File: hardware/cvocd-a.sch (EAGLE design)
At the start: 123 parts, among them IC1 LPC812, IC2 AD5696R, IC3 MC14094B, IC4 MC14094B, IC5 LM324D, IC6 REG1117, IC7 6N138, IC8 24LC_64T-I/OT, IC9 MIC5504-2.8YM5-TR

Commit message: rename
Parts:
- removed ACT, PWR, STA: (no value), led:LED3MM
- removed C22: (no value), resistor:CPOL-EUE2.5-5
- removed C23: 100n, rcl:C-EUC0805
- removed C24, C25: (no value), rcl:C-EUC0805
- removed D3, D4, D5: (no value), microbuilder:DIODESOD-123
- removed GT1, GT10, GT11, GT12, GT2, GT3, GT4, GT5, GT6, GT7, GT8, GT9: VERTICAL_3_5MM_SOCKET, jason_eagle6:VERTICAL_3_5MM_SOCKET
- removed IC8: 24LC_64T-I/OT, Microchip-24LCxxx:24LC_64T-I/OT
- removed IC9: MIC5504-2.8YM5-TR, jason_eagle6:MIC5504-2.8YM5-TR
- removed MODE: (no value), switch-omron:10-XX
- removed Q1, Q11, Q13, Q2, Q7, Q9: (no value), microbuilder:MOSFET-P
- removed Q10, Q12, Q14, Q8: (no value), transistor:MMBT3904LT1-NPN-SOT23-BEC
- removed Q3, Q4, Q5, Q6: (no value), jason_eagle6:MOSFET-N_DUAL
- removed R30, R31, R32, R33, R34, R35, R36, R37, R38, R39, R40, R41, R42, R43, R44, R45, R46, R47: (no value), rcl:R-EU_R0805
- added D2: 1N4004, jasons_stuff:1N4004
- added GATE1, GATE10, GATE11, GATE12, GATE2, GATE3, GATE4, GATE5, GATE6, GATE7, GATE8, GATE9: VERTICAL_3_5MM_SOCKET, jason_eagle6:VERTICAL_3_5MM_SOCKET
- added L1, L2, L3: (no value), led:LED3MM
- added S1: (no value), switch-omron:10-XX
- C10, C14, C15: value 100n -> (none)
- C16: device microbuilder:CAP_TANTALUMA/3216_REFLOW -> rcl:C-EUC0805
- C18, C19, C9: value (none) -> 100n
- C20: device rcl:C-EUC0805 -> resistor:CPOL-EUE2.5-5
- IC1: value LPC812 -> PIC16F1825SO14; device jason_eagle6:LPC812 -> jasons_stuff:PIC16F1825SO14
- IC2: value AD5696R -> 74HC595D; device jason_eagle6:AD5696R -> 74xx-eu:74HC595D
- IC3: value MC14094B -> 74HC595D; device jason_eagle6:MC14094B -> 74xx-eu:74HC595D
- IC4: value MC14094B -> MCP4728_QUAD_DAC; device jason_eagle6:MC14094B -> jason_eagle6:MCP4728_QUAD_DAC
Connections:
- removed net 12V: C11.2, C14.1, C22.+, D5.C, IC5P.V+, IC6.VIN, Q1.S, Q2.S, R36.2, R37.2
- removed net 3V3: C15.1, C24.2, IC1.VDD, IC9.VOUT, ICSP.VDD, PWR.A, R4.1
- removed net 5V: C10.1, C16.+, C21.+, C23.1, C25.2, C9.2, D3.A, D4.A, IC2.GAIN, IC2.RESET#, IC2.VDD, IC2.VLOGIC, IC6.VOUT, IC7.VCC, IC8.VCC, IC9.EN, IC9.VIN, R21.1, R22.1, R27.2, R38.2, R39.2
- removed net GT1: C18.1, GT1.4, R40.1, R47.2
- removed net GT1H: IC3.Q4, Q9.G
- removed net GT1L: IC3.Q8, R13.2
- removed net GT1_VSEL: IC1.PIO0_16, Q3G$2.G, R38.1
- removed net GT2: C17.1, GT2.4, R41.1, R44.2
- removed net GT2H: IC3.Q1, Q7.G
- removed net GT2L: IC3.Q5, R14.2
- removed net GT2_VSEL: IC1.PIO0_7, Q3G$1.G, R39.1
- removed net GT3: C20.1, GT3.4, R42.1, R45.2
- removed net GT3H: IC3.Q3, Q13.G
- removed net GT3L: IC3.Q7, R15.2
- removed net GT4: C19.1, GT4.4, R43.1, R46.2
- removed net GT4H: IC3.Q2, Q11.G
- removed net GT4L: IC3.Q6, R16.2
- removed net MODE_SW: IC1.PIO0_17, MODE.S, MODE.S1
- removed net N$10: Q8.B, R14.1
- removed net N$11: Q14.B, R15.1
- removed net N$14: IC3.STROBE, Q6G$2.D, R31.1
- removed net N$17: IC4.Q8, R9.1
- removed net N$18: IC4.Q7, R10.1
- removed net N$19: IC4.Q6, R11.1
- removed net N$38: IC4.Q5, R12.1
- removed net N$44: IC4.Q3, R6.1
- removed net N$45: IC4.Q2, R7.1
- removed net N$54: Q12.C, R46.1
- removed net N$55: Q10.C, R47.1
- removed net N$57: IC1.PIO0_2/TMS, ICSP.ICSP_DAT/PGD
- removed net N$58: IC1.RESET, ICSP.VPP/MCLR, R4.2
- removed net SCL: IC1.PIO0_10, IC2.SCL, IC8.SCL, R22.2
- removed net SDA: IC1.PIO0_11, IC2.SDA, IC8.SDA, R21.2
- removed net VDD_GT1: C13.1, D3.C, IC3.OE, IC3.VDD, Q1.D, Q11.S, Q13.S, Q7.S, Q9.S, R30.2, R31.2, R32.2
- removed net VDD_GT2: C12.1, D4.C, IC4.OE, IC4.VDD, Q2.D, R33.2, R34.2, R35.2
- new net MIDI_OUT: IC1.RC4/TX
- new net N$22: IC1.RC1/SDA/SDI, IC4.SDA, R21.2
- new net N$47: IC2A.QD, R5.1
- new net VDD: C11.2, C12.1, C13.1, C19.2, C20.+, C9.2, IC1.VDD, IC2A.SCL, IC2P.VCC, IC3A.SCL, IC3P.VCC, IC4.VDD, IC6.VOUT, IC7.VCC, ICSP.VDD, L3.A, R21.1, R22.1, R27.2, R4.1
- new net VIN: C10.2, C18.1, C21.+, D2.C, IC5P.V+, IC6.VIN
- net ACT_LED: now also IC1.RA2/INT, L1.A; no longer ACT.A, IC1.PIO0_13
- net GND: now also C10.1, C16.2, C19.1, C20.-, GATE1.2, GATE10.2, GATE11.2, GATE12.2, GATE2.2, GATE3.2, GATE4.2, GATE5.2, GATE6.2, GATE7.2, GATE8.2, GATE9.2, IC2A.G, IC2P.GND, IC3A.G, IC3P.GND, IC4.LDAC#, S1.P, S1.P1; no longer C10.2, C16.-, C19.2, C20.2, C22.-, C23.2, C24.1, C25.1, GT1.2, GT10.2, GT11.2, GT12.2, GT2.2, GT3.2, GT4.2, GT5.2, GT6.2, GT7.2, GT8.2, GT9.2, IC2.A0, IC2.A1, IC2.GND, IC2.LDAC#, IC2.RSTSEL, IC3.VSS, IC8.VSS, IC8.WP, IC9.GND, MODE.P, MODE.P1, Q10.E, Q12.E, Q14.E, Q3G$1.S, Q3G$2.S, Q4G$1.S, Q4G$2.S, Q5G$1.S, Q5G$2.S, Q6G$1.S, Q6G$2.S, Q8.E
- net MIDI_IN: now also IC1.RC5/RX; no longer IC1.PIO0_0
- net N$1: now also C16.1, GATE4.4, R15.2; no longer Q7.D, R41.2
- net N$12: now also IC3A.QA, R15.1; no longer Q12.B, R16.1
- net N$13: now also IC3A.QB, R16.1; no longer Q8.C, R44.1
- net N$15: now also IC3A.QD, R13.1; no longer IC3.DATA, Q6G$1.D, R30.1
- net N$16: now also IC3A.QC, R14.1; no longer IC3.CLOCK, Q5G$1.D, R32.1
- net N$20: now also C4.1, GATE5.4; no longer C8.1, GT9.4
- net N$21: now also IC1.RCO/SCL/SCK, IC4.SCL, R22.2; no longer Q2.G, Q3G$1.D, R37.1
- net N$23: now also C3.1, GATE6.4; no longer C7.1, GT10.4
- net N$24: now also C2.1, GATE7.4; no longer C6.1, GT11.4
- net N$32: now also GATE8.4; no longer GT8.4
- net N$33: now also C8.1, GATE9.4; no longer C4.1, GT5.4
- net N$34: now also IC1.RA3/MCLR#/VPP, ICSP.VPP/MCLR; no longer IC1.PIO0_3/TCK, ICSP.ICSP_CLK/PGC
- net N$35: now also L3.C; no longer PWR.C
- net N$36: now also L1.C; no longer ACT.C
- net N$37: now also L2.C; no longer STA.C
- net N$39: now also C7.1, GATE10.4; no longer C3.1, GT6.4
- net N$4: now also CVA.4; no longer CVC.4
- net N$40: now also D2.A; no longer D5.A
- net N$41: now also C6.1, GATE11.4; no longer C2.1, GT7.4
- net N$43: now also IC2A.QA, R8.1; no longer IC4.Q4, R5.1
- net N$46: now also IC2A.QB, R7.1; no longer IC4.Q1, R8.1
- net N$48: now also IC2A.QC, R6.1; no longer IC4.STROBE, Q5G$2.D, R33.1
- net N$49: now also IC2A.QF, R11.1; no longer IC4.DATA, Q4G$2.D, R34.1
- net N$5: now also CVC.4; no longer CVA.4
- net N$50: now also IC2A.QG, R10.1; no longer IC4.CLOCK, Q4G$1.D, R35.1
- net N$51: now also IC2A.QE, R12.1; no longer Q14.C, R45.1
- net N$52: now also GATE12.4; no longer GT12.4
- net N$53: now also IC2A.QH, R9.1; no longer Q9.D, R40.2
- net N$6: now also C17.1, GATE3.4, R16.2; no longer Q13.D, R42.2
- net N$7: now also C15.1, GATE1.4, R14.2; no longer Q11.D, R43.2
- net N$8: now also C14.1, GATE2.4, R13.2; no longer Q10.B, R13.1
- net N$9: now also IC1.RC3/SS#, R4.2, S1.S, S1.S1; no longer Q1.G, Q3G$2.D, R36.1
- net SR_CLK: now also IC1.RA4/SDO, IC2A.SCK, IC3A.SCK; no longer IC1.PIO0_15, Q4G$1.G, Q5G$1.G
- net SR_DAT: now also IC1.RA0/ICSPDAT, IC3A.SER, ICSP.ICSP_DAT/PGD; no longer IC1.PIO0_9, Q6G$1.G
- net SR_DAT2: now also IC1.RA1/ICPCLK, IC2A.SER, ICSP.ICSP_CLK/PGC; no longer IC1.PIO0_1, Q4G$2.G
- net SR_RCK: now also IC1.RA5, IC2A.RCK, IC3A.RCK; no longer IC1.PIO0_8, Q5G$2.G, Q6G$2.G
- net STATUS_LED: now also IC1.RC2, L2.A; no longer IC1.PIO0_12, STA.A
- net VOUTA: now also IC4.VOUTA, IC5B.+IN; no longer IC2.VOUTA, IC5A.+IN
- net VOUTB: now also IC4.VOUTB, IC5A.+IN; no longer IC2.VOUTB, IC5B.+IN
- net VOUTC: now also IC4.VOUTC; no longer IC2.VOUTC
- net VOUTD: now also IC4.VOUTD; no longer IC2.VOUTD
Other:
- note removed: "0V/5V or 0V/12V outputs depending on supply voltage to shift register"
- note removed: "24LC64T-I/OT 64KBIT"
- note removed: "3.5mm MIDI jack with +5V tip (e.g. Novation/Arturia) can be used as alternative to MIDI DIN input (not both at same time)"
- note removed: "AD5696RARUZ 16-Bit DAC"
- note removed: "CV OUTPUT BUFFERS"
- note removed: "CV OUTPUT DAC"
- note removed: "CV-OCD rev 3 MIDI-TO-CV CONVERTER JASON HOTCHKISS SIXTY FOUR PIXELS LTD"
- note removed: "D3/D4 Schottky Rectifier"
- note removed: "D5 Schottky Rectifier"
- note removed: "GATES 1-4 DRIVE"
- note removed: "GATES 5-12 DRIVE"
- note removed: "GATES VOLTAGE LEVEL SELECT"
- note removed: "LEVEL SHIFT"
- note removed: "LPC812 MCU (CORTEX M0+)"
- note removed: "Logic low input enables 12V supply to gate shift registers."
- note removed: "MC14094BDR2G CMOS Shift Register"
- note removed: "MIDI DATA INPUT"
- note removed: "POWER SUPPLY"
- note removed: "SERIAL EEPROM"
- note removed: "TLV2374QDRG4Q1 Op-Amp R2R"
- note removed: "Tristate outputs 0V/Hi-Z/5V or 0V/Hi-Z/12V depending on supply voltage to shift register IC"
- moved on the sheet: C1, C10, C11, C12, C13, C14, C15, C17, C18, C19, C2, C21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

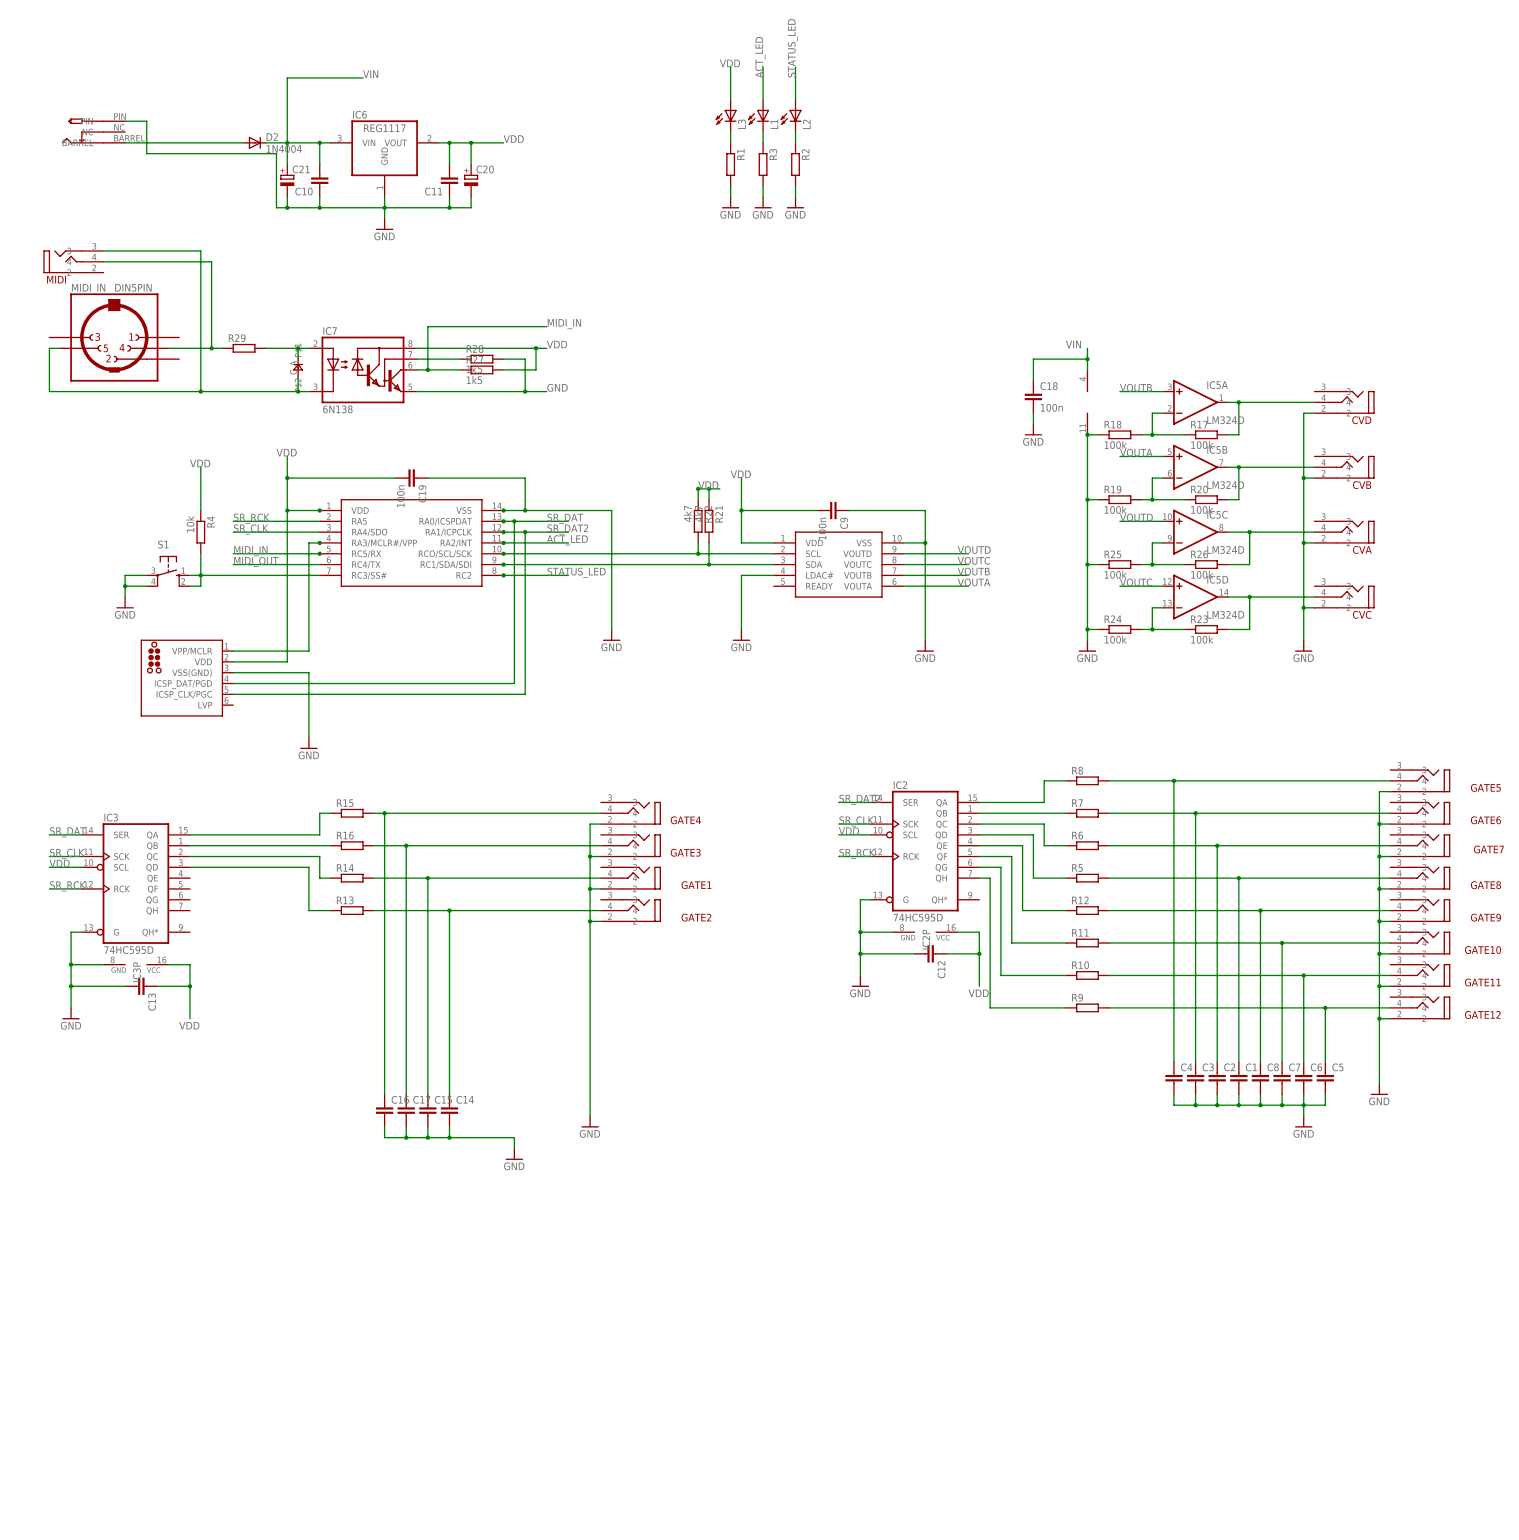
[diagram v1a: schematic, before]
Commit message: smts moved to top of board
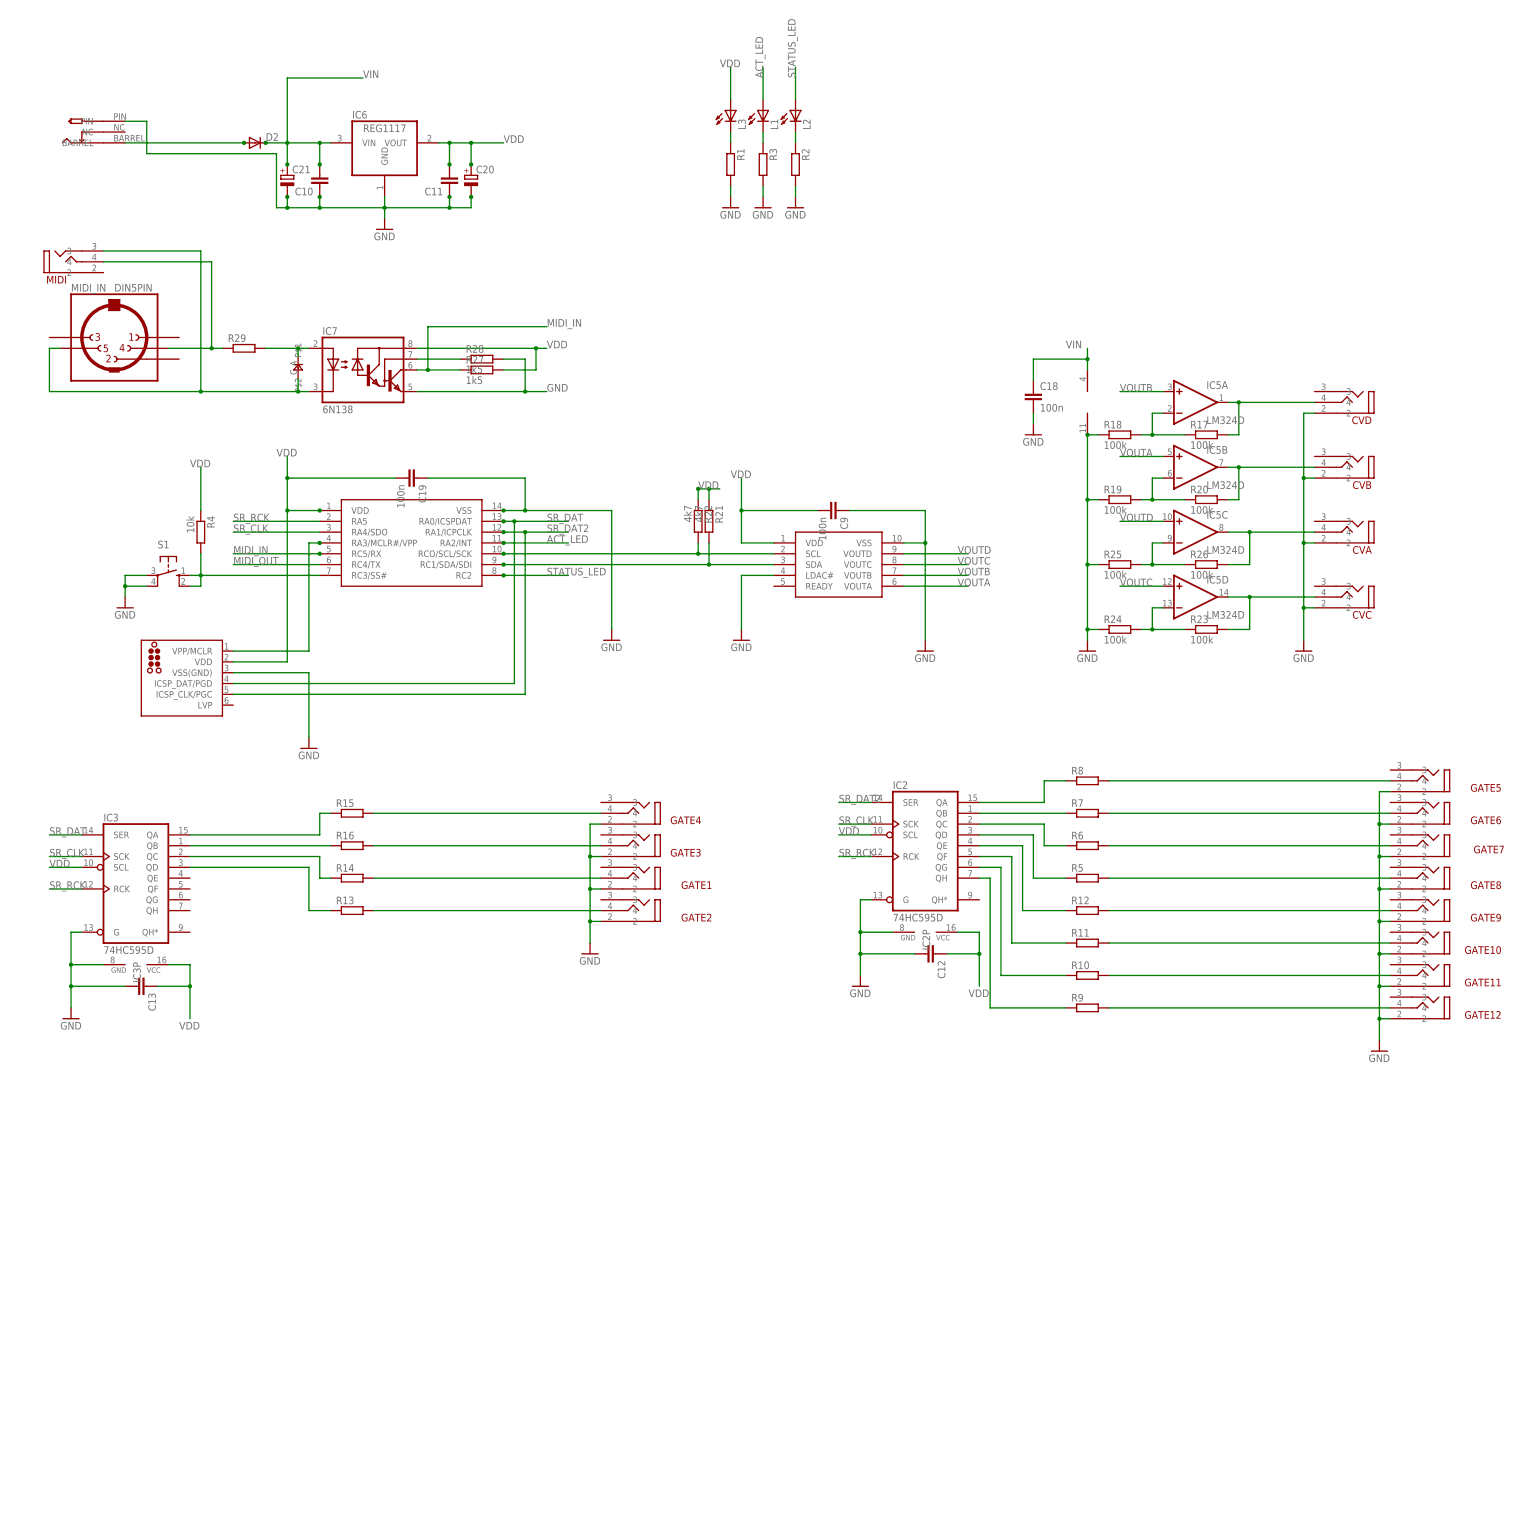
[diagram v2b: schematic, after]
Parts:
- removed C1, C14, C15, C16, C17, C2, C3, C4, C5, C6, C7, C8: (no value), rcl:C-EUC0805
- C20, C21: device resistor:CPOL-EUE2.5-5 -> rcl:CPOL-EUC
- D2: value 1N4004 -> (none); device jasons_stuff:1N4004 -> diode:DIODE-SOD123
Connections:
- net GND: no longer C1.2, C14.2, C15.2, C16.2, C17.2, C2.2, C3.2, C4.2, C5.2, C6.2, C7.2, C8.2
- net N$1: no longer C16.1
- net N$20: no longer C4.1
- net N$23: no longer C3.1
- net N$24: no longer C2.1
- net N$32: no longer C1.1
- net N$33: no longer C8.1
- net N$39: no longer C7.1
- net N$41: no longer C6.1
- net N$52: no longer C5.1
- net N$6: no longer C17.1
- net N$7: no longer C15.1
- net N$8: no longer C14.1
